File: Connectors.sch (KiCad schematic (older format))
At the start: 4 parts

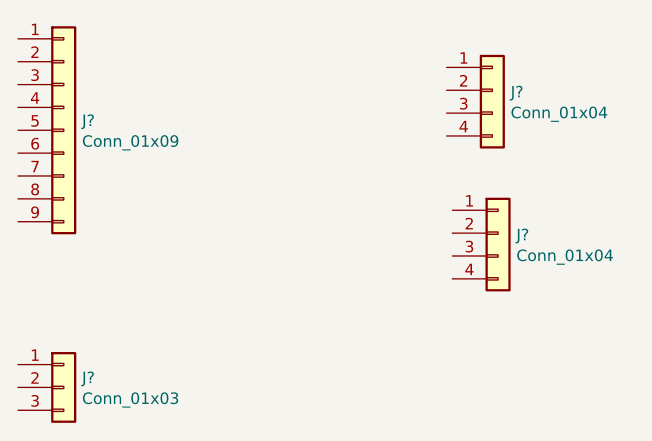
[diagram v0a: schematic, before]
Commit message: annotated symbols
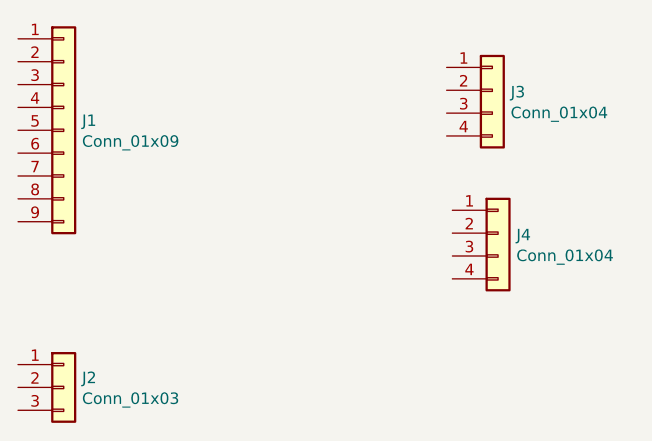
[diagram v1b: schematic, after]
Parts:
- gave numbers to parts that had none: 4
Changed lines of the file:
@@
 $EndDescr
 $Comp
-L Connector_Generic:Conn_01x09 J?
+L Connector_Generic:Conn_01x09 J1
 U 1 1 61A22078
 P 2100 2075
-F 0 "J?" H 2180 2117 50  0000 L CNN
+F 0 "J1" H 2180 2117 50  0000 L CNN
 F 1 "Conn_01x09" H 2180 2026 50  0000 L CNN
 F 2 "" H 2100 2075 50  0001 C CNN
@@
 $EndComp
 $Comp
-L Connector_Generic:Conn_01x04 J?
+L Connector_Generic:Conn_01x04 J3
 U 1 1 61A23633
 P 3975 1900
-F 0 "J?" H 4055 1892 50  0000 L CNN
+F 0 "J3" H 4055 1892 50  0000 L CNN
 F 1 "Conn_01x04" H 4055 1801 50  0000 L CNN
 F 2 "" H 3975 1900 50  0001 C CNN
@@
 $EndComp
 $Comp
-L Connector_Generic:Conn_01x04 J?
+L Connector_Generic:Conn_01x04 J4
 U 1 1 61A23FFF
 P 4000 2525
-F 0 "J?" H 4080 2517 50  0000 L CNN
+F 0 "J4" H 4080 2517 50  0000 L CNN
 F 1 "Conn_01x04" H 4080 2426 50  0000 L CNN
 F 2 "" H 4000 2525 50  0001 C CNN
@@
 $EndComp
 $Comp
-L Connector_Generic:Conn_01x03 J?
+L Connector_Generic:Conn_01x03 J2
 U 1 1 61A24AF0
 P 2100 3200
-F 0 "J?" H 2180 3242 50  0000 L CNN
+F 0 "J2" H 2180 3242 50  0000 L CNN
 F 1 "Conn_01x03" H 2180 3151 50  0000 L CNN
 F 2 "" H 2100 3200 50  0001 C CNN

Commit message: save footprint associations
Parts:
- J1: footprint (none) -> Connector_PinHeader_2.54mm:PinHeader_1x09_P2.54mm_Vertical
- J2: footprint (none) -> Connector_PinHeader_2.54mm:PinHeader_1x03_P2.54mm_Vertical
- J3, J4: footprint (none) -> Connector_PinHeader_2.54mm:PinHeader_1x04_P2.54mm_Vertical
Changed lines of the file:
@@
 F 0 "J1" H 2180 2117 50  0000 L CNN
 F 1 "Conn_01x09" H 2180 2026 50  0000 L CNN
-F 2 "" H 2100 2075 50  0001 C CNN
+F 2 "Connector_PinHeader_2.54mm:PinHeader_1x09_P2.54mm_Vertical" H 2100 2075 50  0001 C CNN
 F 3 "~" H 2100 2075 50  0001 C CNN
 	1    2100 2075
@@
 F 0 "J3" H 4055 1892 50  0000 L CNN
 F 1 "Conn_01x04" H 4055 1801 50  0000 L CNN
-F 2 "" H 3975 1900 50  0001 C CNN
+F 2 "Connector_PinHeader_2.54mm:PinHeader_1x04_P2.54mm_Vertical" H 3975 1900 50  0001 C CNN
 F 3 "~" H 3975 1900 50  0001 C CNN
 	1    3975 1900
@@
 F 0 "J4" H 4080 2517 50  0000 L CNN
 F 1 "Conn_01x04" H 4080 2426 50  0000 L CNN
-F 2 "" H 4000 2525 50  0001 C CNN
+F 2 "Connector_PinHeader_2.54mm:PinHeader_1x04_P2.54mm_Vertical" H 4000 2525 50  0001 C CNN
 F 3 "~" H 4000 2525 50  0001 C CNN
 	1    4000 2525
@@
 F 0 "J2" H 2180 3242 50  0000 L CNN
 F 1 "Conn_01x03" H 2180 3151 50  0000 L CNN
-F 2 "" H 2100 3200 50  0001 C CNN
+F 2 "Connector_PinHeader_2.54mm:PinHeader_1x03_P2.54mm_Vertical" H 2100 3200 50  0001 C CNN
 F 3 "~" H 2100 3200 50  0001 C CNN
 	1    2100 3200

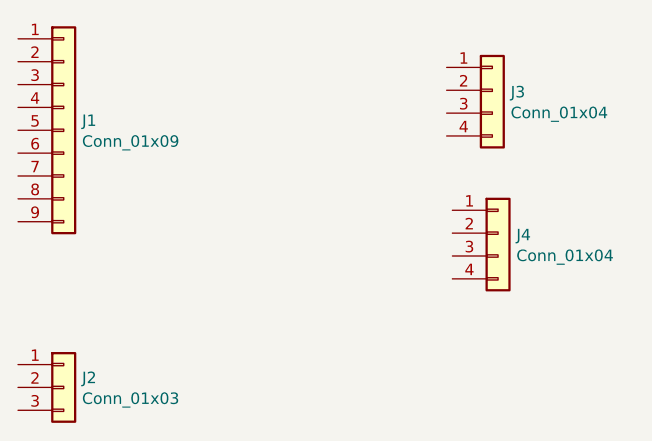
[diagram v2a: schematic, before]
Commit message: save footprint associations
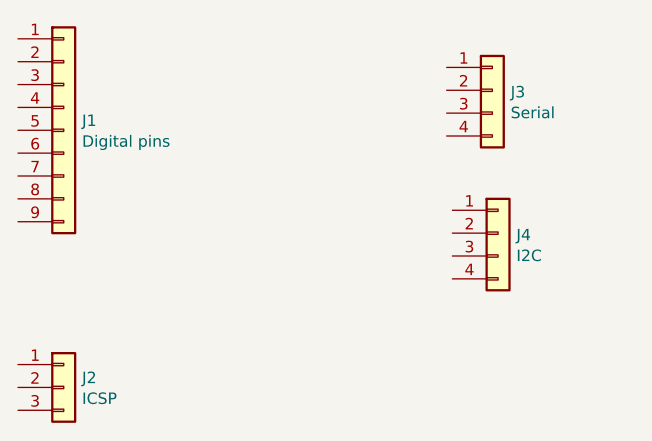
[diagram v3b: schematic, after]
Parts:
- J1: value Conn_01x09 -> Digital pins
- J2: value Conn_01x03 -> ICSP
- J3: value Conn_01x04 -> Serial
- J4: value Conn_01x04 -> I2C
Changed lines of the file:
@@
 P 2100 2075
 F 0 "J1" H 2180 2117 50  0000 L CNN
-F 1 "Conn_01x09" H 2180 2026 50  0000 L CNN
+F 1 "Digital pins" H 2180 2026 50  0000 L CNN
 F 2 "Connector_PinHeader_2.54mm:PinHeader_1x09_P2.54mm_Vertical" H 2100 2075 50  0001 C CNN
 F 3 "~" H 2100 2075 50  0001 C CNN
@@
 P 3975 1900
 F 0 "J3" H 4055 1892 50  0000 L CNN
-F 1 "Conn_01x04" H 4055 1801 50  0000 L CNN
+F 1 "Serial" H 4055 1801 50  0000 L CNN
 F 2 "Connector_PinHeader_2.54mm:PinHeader_1x04_P2.54mm_Vertical" H 3975 1900 50  0001 C CNN
 F 3 "~" H 3975 1900 50  0001 C CNN
@@
 P 4000 2525
 F 0 "J4" H 4080 2517 50  0000 L CNN
-F 1 "Conn_01x04" H 4080 2426 50  0000 L CNN
+F 1 "I2C" H 4080 2426 50  0000 L CNN
 F 2 "Connector_PinHeader_2.54mm:PinHeader_1x04_P2.54mm_Vertical" H 4000 2525 50  0001 C CNN
 F 3 "~" H 4000 2525 50  0001 C CNN
@@
 P 2100 3200
 F 0 "J2" H 2180 3242 50  0000 L CNN
-F 1 "Conn_01x03" H 2180 3151 50  0000 L CNN
+F 1 "ICSP" H 2180 3151 50  0000 L CNN
 F 2 "Connector_PinHeader_2.54mm:PinHeader_1x03_P2.54mm_Vertical" H 2100 3200 50  0001 C CNN
 F 3 "~" H 2100 3200 50  0001 C CNN

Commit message: wiring on connectors sheet
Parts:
- J3: renamed from J2; footprint Connector_PinHeader_2.54mm:PinHeader_1x03_P2.54mm_Vertical -> Connector_PinHeader_2.54mm:PinHeader_2x03_P2.54mm_Vertical; symbol Connector_Generic:Conn_01x03 -> Connector_Generic:Conn_02x03_Odd_Even
- renumbered J3 to J2
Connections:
- net D2: now reaches J1.1 (Pin_1)
- net D3: now reaches J1.2 (Pin_2)
- net D4: now reaches J1.3 (Pin_3)
- net D5: now reaches J1.4 (Pin_4)
- net D6: now reaches J1.5 (Pin_5)
- net D7: now reaches J1.6 (Pin_6)
- net D8: now reaches J1.7 (Pin_7)
- net GND: now reaches J1.8 (Pin_8)
- net GND: now also J2.1 (Pin_1), J3.6 (Pin_6), J4.1 (Pin_1)
- net Vcc: now reaches J1.9 (Pin_9)
- net Vcc: now also J2.2 (Pin_2), J4.2 (Pin_2)
- net RX: now reaches J2.3 (Pin_3)
- net TX: now reaches J2.4 (Pin_4)
- net SDA: now reaches J4.3 (Pin_3)
- net SCK: now reaches J4.4 (Pin_4)
- net SCK: now also J3.3 (Pin_3)
- net MISO: now reaches J3.1 (Pin_1)
- net VCC: now reaches J3.2 (Pin_2)
- new net MOSI: J3.4 (Pin_4)
- new net RESET: J3.5 (Pin_5)
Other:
- moved on the sheet: J1, J2, J4
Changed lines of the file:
@@
 L Connector_Generic:Conn_01x09 J1
 U 1 1 61A22078
-P 2100 2075
-F 0 "J1" H 2180 2117 50  0000 L CNN
-F 1 "Digital pins" H 2180 2026 50  0000 L CNN
-F 2 "Connector_PinHeader_2.54mm:PinHeader_1x09_P2.54mm_Vertical" H 2100 2075 50  0001 C CNN
-F 3 "~" H 2100 2075 50  0001 C CNN
-	1    2100 2075
+P 5000 3225
+F 0 "J1" H 5080 3267 50  0000 L CNN
+F 1 "Digital pins" H 5080 3176 50  0000 L CNN
+F 2 "Connector_PinHeader_2.54mm:PinHeader_1x09_P2.54mm_Vertical" H 5000 3225 50  0001 C CNN
+F 3 "~" H 5000 3225 50  0001 C CNN
+	1    5000 3225
 	1    0    0    -1
 $EndComp
 $Comp
-L Connector_Generic:Conn_01x04 J3
+L Connector_Generic:Conn_01x04 J2
 U 1 1 61A23633
-P 3975 1900
-F 0 "J3" H 4055 1892 50  0000 L CNN
-F 1 "Serial" H 4055 1801 50  0000 L CNN
-F 2 "Connector_PinHeader_2.54mm:PinHeader_1x04_P2.54mm_Vertical" H 3975 1900 50  0001 C CNN
-F 3 "~" H 3975 1900 50  0001 C CNN
-	1    3975 1900
+P 6875 3050
+F 0 "J2" H 6955 3042 50  0000 L CNN
+F 1 "Serial" H 6955 2951 50  0000 L CNN
+F 2 "Connector_PinHeader_2.54mm:PinHeader_1x04_P2.54mm_Vertical" H 6875 3050 50  0001 C CNN
+F 3 "~" H 6875 3050 50  0001 C CNN
+	1    6875 3050
 	1    0    0    -1
 $EndComp
@@
 L Connector_Generic:Conn_01x04 J4
 U 1 1 61A23FFF
-P 4000 2525
-F 0 "J4" H 4080 2517 50  0000 L CNN
-F 1 "I2C" H 4080 2426 50  0000 L CNN
-F 2 "Connector_PinHeader_2.54mm:PinHeader_1x04_P2.54mm_Vertical" H 4000 2525 50  0001 C CNN
-F 3 "~" H 4000 2525 50  0001 C CNN
-	1    4000 2525
+P 6900 3675
+F 0 "J4" H 6980 3667 50  0000 L CNN
+F 1 "I2C" H 6980 3576 50  0000 L CNN
+F 2 "Connector_PinHeader_2.54mm:PinHeader_1x04_P2.54mm_Vertical" H 6900 3675 50  0001 C CNN
+F 3 "~" H 6900 3675 50  0001 C CNN
+	1    6900 3675
 	1    0    0    -1
 $EndComp
 $Comp
-L Connector_Generic:Conn_01x03 J2
+L Connector_Generic:Conn_02x03_Odd_Even J3
 U 1 1 61A24AF0
-P 2100 3200
-F 0 "J2" H 2180 3242 50  0000 L CNN
-F 1 "ICSP" H 2180 3151 50  0000 L CNN
-F 2 "Connector_PinHeader_2.54mm:PinHeader_1x03_P2.54mm_Vertical" H 2100 3200 50  0001 C CNN
-F 3 "~" H 2100 3200 50  0001 C CNN
-	1    2100 3200
+P 5000 4350
+F 0 "J3" H 5000 4625 50  0000 L CNN
+F 1 "ICSP" H 4975 4550 50  0000 L CNN
+F 2 "Connector_PinHeader_2.54mm:PinHeader_2x03_P2.54mm_Vertical" H 5000 4350 50  0001 C CNN
+F 3 "~" H 5000 4350 50  0001 C CNN
+	1    5000 4350
 	1    0    0    -1
 $EndComp
+Text HLabel 4800 4250 0    50   Output ~ 0
+MISO
+Text HLabel 4800 4350 0    50   BiDi ~ 0
+SCK
+Text HLabel 4800 4450 0    50   Output ~ 0
+RESET
+Text HLabel 5300 4250 2    50   Input ~ 0
+VCC
+Text HLabel 5300 4350 2    50   Input ~ 0
+MOSI
+Text HLabel 5300 4450 2    50   Input ~ 0
+GND
+Text HLabel 6675 2950 0    50   Input ~ 0
+GND
+Text HLabel 6675 3050 0    50   Input ~ 0
+Vcc
+Text HLabel 6675 3150 0    50   Input ~ 0
+RX
+Text HLabel 6675 3250 0    50   Output ~ 0
+TX
+Text HLabel 6700 3575 0    50   Input ~ 0
+GND
+Text HLabel 6700 3675 0    50   Input ~ 0
+Vcc
+Text HLabel 6700 3775 0    50   Input ~ 0
+SDA
+Text HLabel 6700 3875 0    50   Output ~ 0
+SCK
+Text HLabel 4800 2825 0    50   BiDi ~ 0
+D2
+Text HLabel 4800 2925 0    50   BiDi ~ 0
+D3
+Text HLabel 4800 3025 0    50   BiDi ~ 0
+D4
+Text HLabel 4800 3125 0    50   BiDi ~ 0
+D5
+Text HLabel 4800 3225 0    50   BiDi ~ 0
+D6
+Text HLabel 4800 3325 0    50   BiDi ~ 0
+D7
+Text HLabel 4800 3425 0    50   BiDi ~ 0
+D8
+Text HLabel 4800 3525 0    50   Input ~ 0
+GND
+Text HLabel 4800 3625 0    50   Input ~ 0
+Vcc
 $EndSCHEMATC

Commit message: added comments
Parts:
- renumbered J4 to J2, J1 to J3, J2 to J4, J3 to J5
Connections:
- net VCC is gone; now on net Vcc: J5.2 (Pin_2)
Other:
- note added: "N5 - I2C connector"
- note added: "N6 - Serial connector"
- note added: "N7 - GPIO connector"
- note added: "N8 - SPI connector"
- moved on the sheet: J2, J3, J4, J5
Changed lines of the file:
@@
 $EndDescr
 $Comp
-L Connector_Generic:Conn_01x09 J1
+L Connector_Generic:Conn_01x09 J3
 U 1 1 61A22078
-P 5000 3225
-F 0 "J1" H 5080 3267 50  0000 L CNN
-F 1 "Digital pins" H 5080 3176 50  0000 L CNN
-F 2 "Connector_PinHeader_2.54mm:PinHeader_1x09_P2.54mm_Vertical" H 5000 3225 50  0001 C CNN
-F 3 "~" H 5000 3225 50  0001 C CNN
-	1    5000 3225
+P 5125 4025
+F 0 "J3" H 5205 4067 50  0000 L CNN
+F 1 "Digital pins" H 5205 3976 50  0000 L CNN
+F 2 "Connector_PinHeader_2.54mm:PinHeader_1x09_P2.54mm_Vertical" H 5125 4025 50  0001 C CNN
+F 3 "~" H 5125 4025 50  0001 C CNN
+	1    5125 4025
+	1    0    0    -1
+$EndComp
+$Comp
+L Connector_Generic:Conn_01x04 J4
+U 1 1 61A23633
+P 6800 2850
+F 0 "J4" H 6880 2842 50  0000 L CNN
+F 1 "Serial" H 6880 2751 50  0000 L CNN
+F 2 "Connector_PinHeader_2.54mm:PinHeader_1x04_P2.54mm_Vertical" H 6800 2850 50  0001 C CNN
+F 3 "~" H 6800 2850 50  0001 C CNN
+	1    6800 2850
 	1    0    0    -1
 $EndComp
 $Comp
 L Connector_Generic:Conn_01x04 J2
-U 1 1 61A23633
-P 6875 3050
-F 0 "J2" H 6955 3042 50  0000 L CNN
-F 1 "Serial" H 6955 2951 50  0000 L CNN
-F 2 "Connector_PinHeader_2.54mm:PinHeader_1x04_P2.54mm_Vertical" H 6875 3050 50  0001 C CNN
-F 3 "~" H 6875 3050 50  0001 C CNN
-	1    6875 3050
+U 1 1 61A23FFF
+P 5150 2850
+F 0 "J2" H 5230 2842 50  0000 L CNN
+F 1 "I2C" H 5230 2751 50  0000 L CNN
+F 2 "Connector_PinHeader_2.54mm:PinHeader_1x04_P2.54mm_Vertical" H 5150 2850 50  0001 C CNN
+F 3 "~" H 5150 2850 50  0001 C CNN
+	1    5150 2850
 	1    0    0    -1
 $EndComp
 $Comp
-L Connector_Generic:Conn_01x04 J4
-U 1 1 61A23FFF
-P 6900 3675
-F 0 "J4" H 6980 3667 50  0000 L CNN
-F 1 "I2C" H 6980 3576 50  0000 L CNN
-F 2 "Connector_PinHeader_2.54mm:PinHeader_1x04_P2.54mm_Vertical" H 6900 3675 50  0001 C CNN
-F 3 "~" H 6900 3675 50  0001 C CNN
-	1    6900 3675
+L Connector_Generic:Conn_02x03_Odd_Even J5
+U 1 1 61A24AF0
+P 6750 3875
+F 0 "J5" H 6750 4150 50  0000 L CNN
+F 1 "ICSP" H 6725 4075 50  0000 L CNN
+F 2 "Connector_PinHeader_2.54mm:PinHeader_2x03_P2.54mm_Vertical" H 6750 3875 50  0001 C CNN
+F 3 "~" H 6750 3875 50  0001 C CNN
+	1    6750 3875
 	1    0    0    -1
 $EndComp
-$Comp
-L Connector_Generic:Conn_02x03_Odd_Even J3
-U 1 1 61A24AF0
-P 5000 4350
-F 0 "J3" H 5000 4625 50  0000 L CNN
-F 1 "ICSP" H 4975 4550 50  0000 L CNN
-F 2 "Connector_PinHeader_2.54mm:PinHeader_2x03_P2.54mm_Vertical" H 5000 4350 50  0001 C CNN
-F 3 "~" H 5000 4350 50  0001 C CNN
-	1    5000 4350
-	1    0    0    -1
-$EndComp
-Text HLabel 4800 4250 0    50   Output ~ 0
+Text HLabel 6550 3775 0    50   Output ~ 0
 MISO
-Text HLabel 4800 4350 0    50   BiDi ~ 0
+Text HLabel 6550 3875 0    50   BiDi ~ 0
 SCK
-Text HLabel 4800 4450 0    50   Output ~ 0
+Text HLabel 7050 3775 2    50   Input ~ 0
+Vcc
+Text HLabel 7050 3875 2    50   Input ~ 0
+MOSI
+Text HLabel 7050 3975 2    50   Input ~ 0
+GND
+Text HLabel 6600 2750 0    50   Input ~ 0
+GND
+Text HLabel 6600 2850 0    50   Input ~ 0
+Vcc
+Text HLabel 6600 2950 0    50   Input ~ 0
+RX
+Text HLabel 6600 3050 0    50   Output ~ 0
+TX
+Text HLabel 4950 2750 0    50   Input ~ 0
+GND
+Text HLabel 4950 2850 0    50   Input ~ 0
+Vcc
+Text HLabel 4950 2950 0    50   Input ~ 0
+SDA
+Text HLabel 4950 3050 0    50   Output ~ 0
+SCK
+Text HLabel 4925 3625 0    50   BiDi ~ 0
+D2
+Text HLabel 4925 3725 0    50   BiDi ~ 0
+D3
+Text HLabel 4925 3825 0    50   BiDi ~ 0
+D4
+Text HLabel 4925 3925 0    50   BiDi ~ 0
+D5
+Text HLabel 4925 4025 0    50   BiDi ~ 0
+D6
+Text HLabel 4925 4125 0    50   BiDi ~ 0
+D7
+Text HLabel 4925 4225 0    50   BiDi ~ 0
+D8
+Text HLabel 4925 4325 0    50   Input ~ 0
+GND
+Text HLabel 4925 4425 0    50   Input ~ 0
+Vcc
+Text HLabel 6550 3975 0    50   Input ~ 0
 RESET
-Text HLabel 5300 4250 2    50   Input ~ 0
-VCC
-Text HLabel 5300 4350 2    50   Input ~ 0
-MOSI
-Text HLabel 5300 4450 2    50   Input ~ 0
-GND
-Text HLabel 6675 2950 0    50   Input ~ 0
-GND
-Text HLabel 6675 3050 0    50   Input ~ 0
-Vcc
-Text HLabel 6675 3150 0    50   Input ~ 0
-RX
-Text HLabel 6675 3250 0    50   Output ~ 0
-TX
-Text HLabel 6700 3575 0    50   Input ~ 0
-GND
-Text HLabel 6700 3675 0    50   Input ~ 0
-Vcc
-Text HLabel 6700 3775 0    50   Input ~ 0
-SDA
-Text HLabel 6700 3875 0    50   Output ~ 0
-SCK
-Text HLabel 4800 2825 0    50   BiDi ~ 0
-D2
-Text HLabel 4800 2925 0    50   BiDi ~ 0
-D3
-Text HLabel 4800 3025 0    50   BiDi ~ 0
-D4
-Text HLabel 4800 3125 0    50   BiDi ~ 0
-D5
-Text HLabel 4800 3225 0    50   BiDi ~ 0
-D6
-Text HLabel 4800 3325 0    50   BiDi ~ 0
-D7
-Text HLabel 4800 3425 0    50   BiDi ~ 0
-D8
-Text HLabel 4800 3525 0    50   Input ~ 0
-GND
-Text HLabel 4800 3625 0    50   Input ~ 0
-Vcc
+Text Notes 4675 2550 0    50   ~ 0
+N5 - I2C connector
+Text Notes 6375 2550 0    50   ~ 0
+N6 - Serial connector
+Text Notes 4675 3450 0    50   ~ 0
+N7 - GPIO connector
+Text Notes 6375 3475 0    50   ~ 0
+N8 - SPI connector
 $EndSCHEMATC
